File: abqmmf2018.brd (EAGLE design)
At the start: 125.5 x 93.7 mm, 14 parts

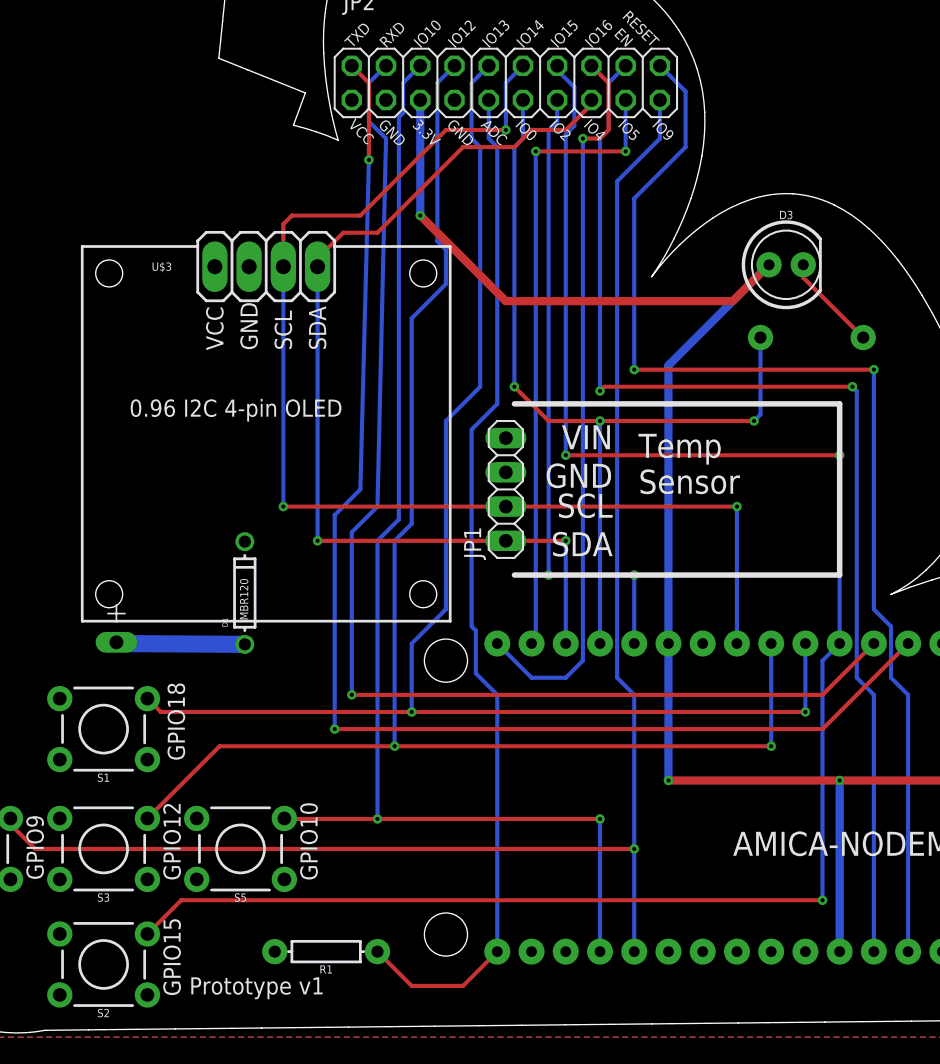
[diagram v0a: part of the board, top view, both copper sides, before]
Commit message: Moving Screen & Sensor, Remove ADC Resistor
Moving the Sensor more right since it's smaller than I had
somewhat expected, so that's nice.  Moved the screen so that
it's more inside the cloud.

Obviously had to do some rerouting to accomodate.  Like it a
little better anyway.

Also removed the ADC voltage divider resistor.  Turns out
you can muck with the boot firmware enough to flip the ADC
line to measure a 3.3V VDD value.  This seems to return about
2.9V with a full battery, and will go until it hits about
1.53V-ish before the NodeMCU just falls over.  Amusingly the
OLED screen (on my test) kept going.
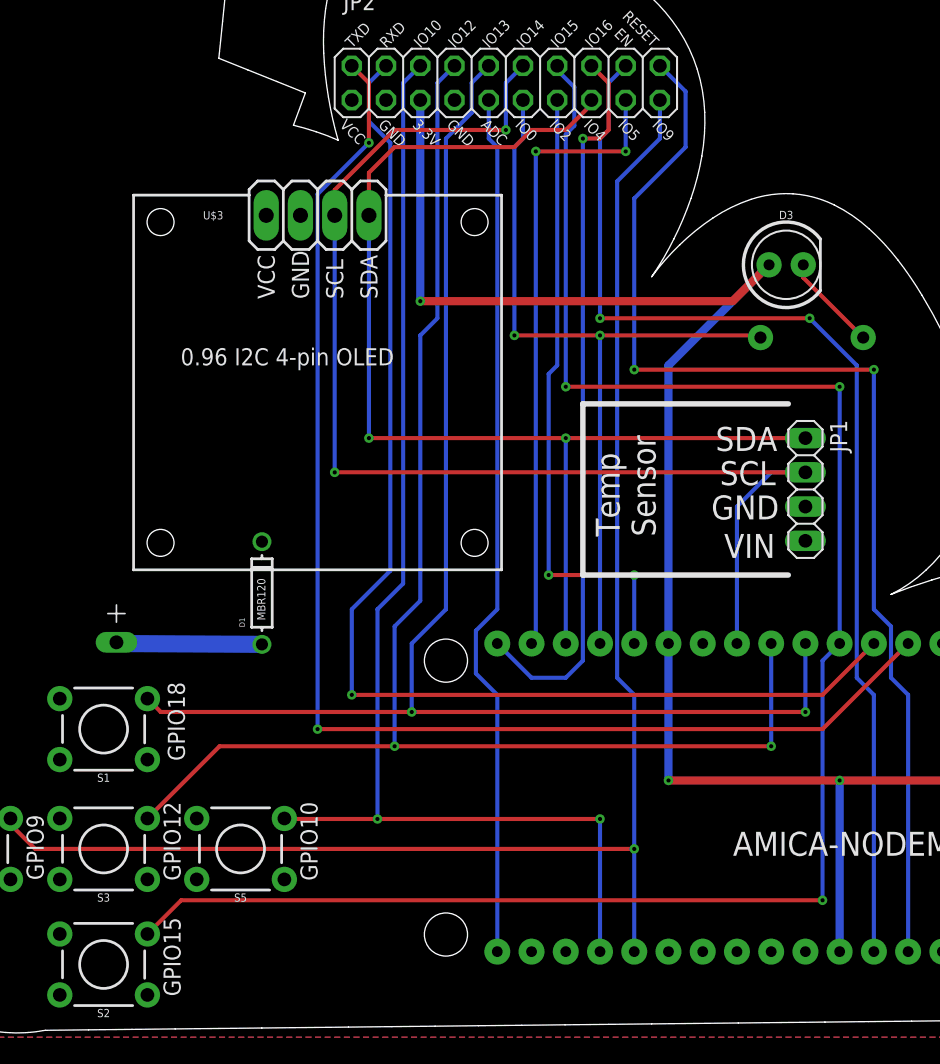
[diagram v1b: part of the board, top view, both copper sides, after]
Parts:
- removed R1: 420k, SparkFun-Resistors:AXIAL-0.3
- moved JP1 22.2 mm to (99.1, 40.6), turned to 270 degrees
- moved U$3 5.39 mm to (62.9, 48.6)
- moved D1 1.27 mm to (58.7, 33.0)
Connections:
- net ADC: no longer R1.P$1
- net VCC: no longer R1.P$2
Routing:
- net GPIO4/SDA: track 72.4 -> 86.2 mm
- net ADC: track 76.0 -> 64.8 mm
- net GPIO0: track 63.3 -> 58.9 mm, vias 3 -> 2
- net 3.3V: track 125.3 -> 129.0 mm
- net GPIO14/SCK: track 89.5 -> 92.0 mm, vias 3 -> 2
- net EN: track 86.4 -> 84.0 mm
- net TXD: track 95.7 -> 97.8 mm
- net N$1: track 9.56 -> 10.8 mm
- net GPIO13/MOSI: track 105.1 -> 104.6 mm
- net GPIO12/MISO: track 109.0 -> 108.4 mm
- net RXD: track 88.8 -> 89.4 mm
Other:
- board text added: "(C) John 'Warthog9' Hawley 2018 CC-BY-SA Artwork by Dr. Terri Oda Board Version: 1.1"
- board text removed: "(C) John 'Warthog9' Hawley 2018 CC-BY-SA Artwork by Dr. Terri Oda"
- board text removed: "Prototype v1"
